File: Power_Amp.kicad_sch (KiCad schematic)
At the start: 22 parts, among them J10 PIC-S-203F, J11 Molex 73251-1153, P13 CONUFL001-SMD-T, U27 TQP7M9106

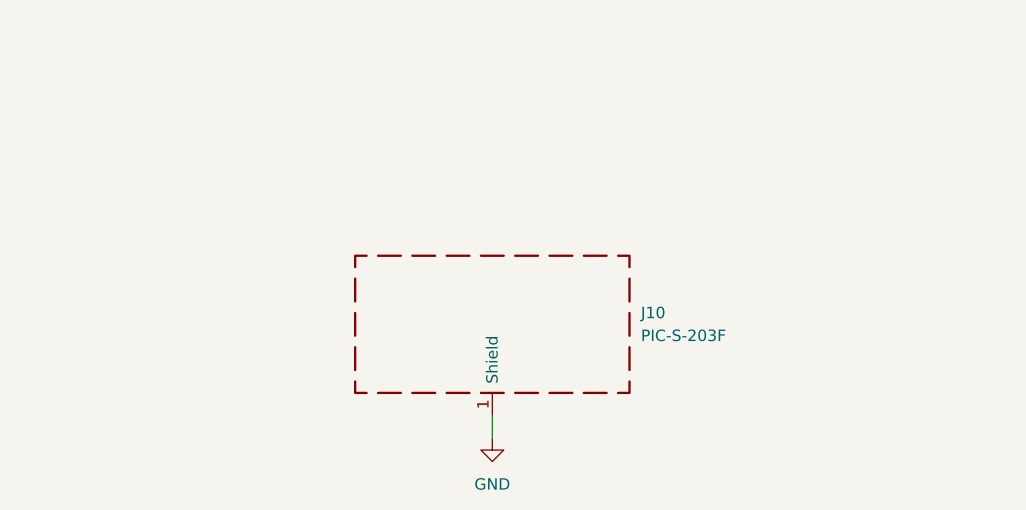
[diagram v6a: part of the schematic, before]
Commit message: Change to aluminum shielding
Signed-off-by: Corey Minyard <corey@minyard.net>
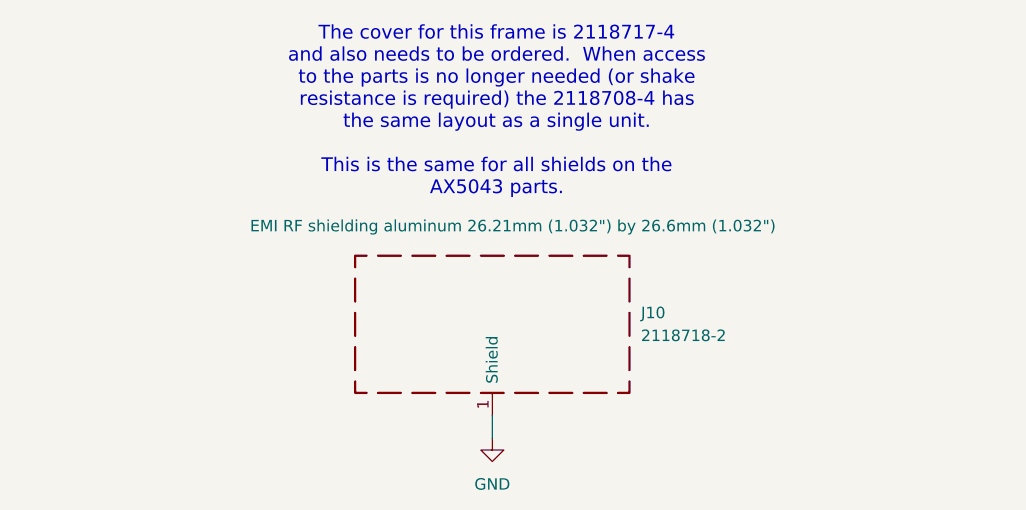
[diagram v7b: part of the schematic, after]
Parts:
- J10: value PIC-S-203F -> 2118718-2
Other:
- note added: "The cover for this frame is 2118717-4 and also needs to be ordered. When access to the parts is no longer needed (or shake resistance is required) the 2118708-4 has the same layout as a single unit. This is the same for all shields on the AX5043 parts."
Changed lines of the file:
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@@
 		(comment 1 "N5BRG")
+	)
+	(text "The cover for this frame is 2118717-4\nand also needs to be ordered.  When access\nto the parts is no longer needed (or shake\nresistance is required) the 2118708-4 has\nthe same layout as a single unit.\n\nThis is the same for all shields on the\nAX5043 parts."
+		(exclude_from_sim no)
+		(at 105.918 24.638 0)
+		(effects
+			(font
+				(size 1.524 1.524)
+			)
+		)
 	)
 	(text "Inductor to bleed of static build\nup on the antenna."
@@
 		(on_board yes)
 		(dnp no)
-		(fields_autoplaced yes)
 		(property "Reference" "J10"
 			(at 121.92 46.9899 0)
@@
 			)
 		)
-		(property "Value" "PIC-S-203F"
+		(property "Value" "2118718-2"
 			(at 121.92 49.5299 0)
 			(effects
@@
 			)
 		)
-		(property "Description" "One-piece EMI RF shielding cabinet"
-			(at 105.41 48.26 0)
-			(effects
-				(font
-					(size 1.27 1.27)
-				)
-				(hide yes)
-			)
-		)
+		(property "Description" "EMI RF shielding aluminum 26.21mm (1.032\") by 26.6mm (1.032\")"
+			(at 107.696 37.338 0)
+			(effects
+				(font
+					(size 1.27 1.27)
+				)
+			)
+		)

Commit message: More shield work
Signed-off-by: Corey Minyard <corey@minyard.net>
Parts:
- removed J10: 2118718-2, PacSatDev_misc:RF_SHIELD_PIC_S_203, symbol Device:RFShield_OnePiece
- added J10: 2118718-2, PacSatDev_misc:TE_2118718-2, symbol PACSAT_DEV_misc:2118718-2
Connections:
- net GND: now also J10.SH1 (SHIELD), J10.SH10 (SHIELD__9), J10.SH11 (SHIELD__10), J10.SH12 (SHIELD__11), J10.SH13 (SHIELD__12), J10.SH14 (SHIELD__13), J10.SH15 (SHIELD__14), J10.SH16 (SHIELD__15), J10.SH2 (SHIELD__1), J10.SH3 (SHIELD__2), J10.SH4 (SHIELD__3), J10.SH5 (SHIELD__4), J10.SH6 (SHIELD__5), J10.SH7 (SHIELD__6), J10.SH8 (SHIELD__7), J10.SH9 (SHIELD__8)
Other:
- note added: "The cover for this frame is 2118717-4 and also needs to be ordered. When access to the parts is no longer needed (or shake resistance is required) the 2118708-4 has the same layout as a single unit."
- note removed: "The cover for this frame is 2118717-4 and also needs to be ordered. When access to the parts is no longer needed (or shake resistance is required) the 2118708-4 has the same layout as a single unit. This is the same for all shields on the AX5043 parts."
